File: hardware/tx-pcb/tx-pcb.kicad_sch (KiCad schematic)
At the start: 0 parts

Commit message: WIP TX Board
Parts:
- added C1, C11, C17, C2, C3, C4, C5, C8: 100n, symbol Device:C
- added C12, C6, C7: 4u7, symbol Device:C
- added C13: 100p, symbol Device:C
- added C14, C15: C, symbol Device:C
- added C16: 1u, symbol Device:C
- added FL1: MLPF-WB55-01E3, easyeda2kicad:FILTER-SMD_6P-L1.6-W1.0-P0.50-BL, symbol easyeda2kicad:MLPF-WB55-01E3
- added J1: TC2030, Connector:Tag-Connect_TC2030-IDC-FP_2x03_P1.27mm_Vertical, symbol Connector:Conn_ARM_SWD_TagConnect_TC2030
- added J2: CC1101_RF_Module_Conn, symbol Connector_Generic:Conn_02x04_Odd_Even
- added J3: USB2.0_C_16P, symbol Connector:USB_C_Receptacle_USB2.0_16P
- added L1: 10n, symbol Device:L
- added L2: 10u, symbol Device:L
- added R1, R3, R4: 5k1, symbol Device:R
- added R2: 100R, symbol Device:R
- added SW1: SW_Push, symbol Switch:SW_Push
- added U1: STM32WB55CEUx, Package_DFN_QFN:QFN-48-1EP_7x7mm_P0.5mm_EP5.6x5.6mm, symbol MCU_ST_STM32WB:STM32WB55CEUx
- added U2: USBLC6-2SC6, Package_TO_SOT_SMD:SOT-23-6, symbol Power_Protection:USBLC6-2SC6
- added X1: NX2016SA-32MHZ-STD-CZS-5, easyeda2kicad:OSC-SMD_4P-L2.0-W1.6-BL, symbol easyeda2kicad:NX2016SA-32MHZ-STD-CZS-5
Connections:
- new net: J3.A5 (CC1), R4.1
- new net: J3.A6 (D+), J3.B6 (D+), U2.3 (I/O2)
- new net: J3.A7 (D-), J3.B7 (D-), U2.1 (I/O1)
- new net: J3.B5 (CC2), R3.1
- new net: R2.2, SW1.1
- new net: J1.2 (SWDIO), U1.39 (PA13)
- new net: J1.4 (SWCLK), U1.41 (PA14)
- new net: J1.6 (SWO), U1.43 (PB3)
- new net +3V3: C1.1, C11.1, C13.1, C2.1, C3.1, C4.1, C5.1, C6.1, C7.1, C8.1, J1.1 (VCC), J2.2 (Pin_2), SW1.2, U1.1 (VBAT), U1.20 (VDD), U1.23 (VDDRF), U1.34 (VDDSMPS), U1.35 (VDD), U1.40 (VDDUSB), U1.48 (VDD), U1.8 (VDDA)
- new net +5V: J3.A4 (VBUS), J3.A9 (VBUS), J3.B4 (VBUS), J3.B9 (VBUS), U2.5 (VBUS)
- new net BOOT0: C17.2, R1.1, R2.1, U1.4 (PH3)
- new net C1101_CSN: J2.4 (Pin_4)
- new net C1101_GD02: J2.8 (Pin_8)
- new net C1101_GDO0: J2.3 (Pin_3)
- new net C1101_MISO/GD01: J2.7 (Pin_7)
- new net C1101_MOSI: J2.6 (Pin_6)
- new net C1101_SCK: J2.5 (Pin_5)
- new net GND: C1.2, C11.2, C12.2, C13.2, C14.2, C15.2, C16.2, C17.1, C2.2, C3.2, C4.2, C5.2, C6.2, C7.2, C8.2, FL1.2 (GND4), FL1.4 (GND1), FL1.5 (GND2), FL1.6 (GND3), J1.5 (GND), J2.1 (Pin_1), J3.A1 (GND), J3.A12 (GND), J3.B1 (GND), J3.B12 (GND), J3.SH (SHIELD), R1.2, R3.2, R4.2, U1.22 (VSSRF), U1.32 (VSSSMPS), U1.49 (VSS), U2.2 (GND), X1.2 (GND), X1.4 (GND)
- new net HSE_OSC_IN: U1.25 (OSC_IN), X1.1
- new net HSE_OSC_OUT: U1.24 (OSC_OUT), X1.3
- new net LSE_OSC_IN: C15.1, U1.2 (PC14)
- new net LSE_OSC_OUT: C14.1, U1.3 (PC15)
- new net RF1_IN: FL1.3 (IN), U1.21 (RF1)
- new net SMPSFB: C12.1, L2.2, U1.31 (VFBSMPS)
- new net SMPSLX: L1.1, U1.33 (VLXSMPS)
- new net SMPSLXL: L1.2, L2.1
- new net SWD_NSRT: C16.1, J1.3 (~{RESET}), U1.7 (NRST)
- new net USB_DM: U1.37 (PA11), U2.6 (I/O1)
- new net USB_DP: U1.38 (PA12), U2.4 (I/O2)
- no-connect marks 0 -> 2
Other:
- added sheet Power (Power.kicad_sch)
- note added: "5k1 R's tell the computer there is a power-sinking device connected"
- note added: "ESD Protection"
- note added: "From STM application note an5165 STM32WB55xx 6.1.6 Fig 16"
- note added: "MLFP-WB55-01D3 / -01E3 ?"
- note added: "Refer to AN6335 for trace Z"
- note added: "ST DESIGN NOTE AN2867"
- note added: "debounce; det vals"
- note added: "match with TX?"
- company: (none) -> University of Central Florida Student Group
- title: (none) -> Transceiver Demo Board

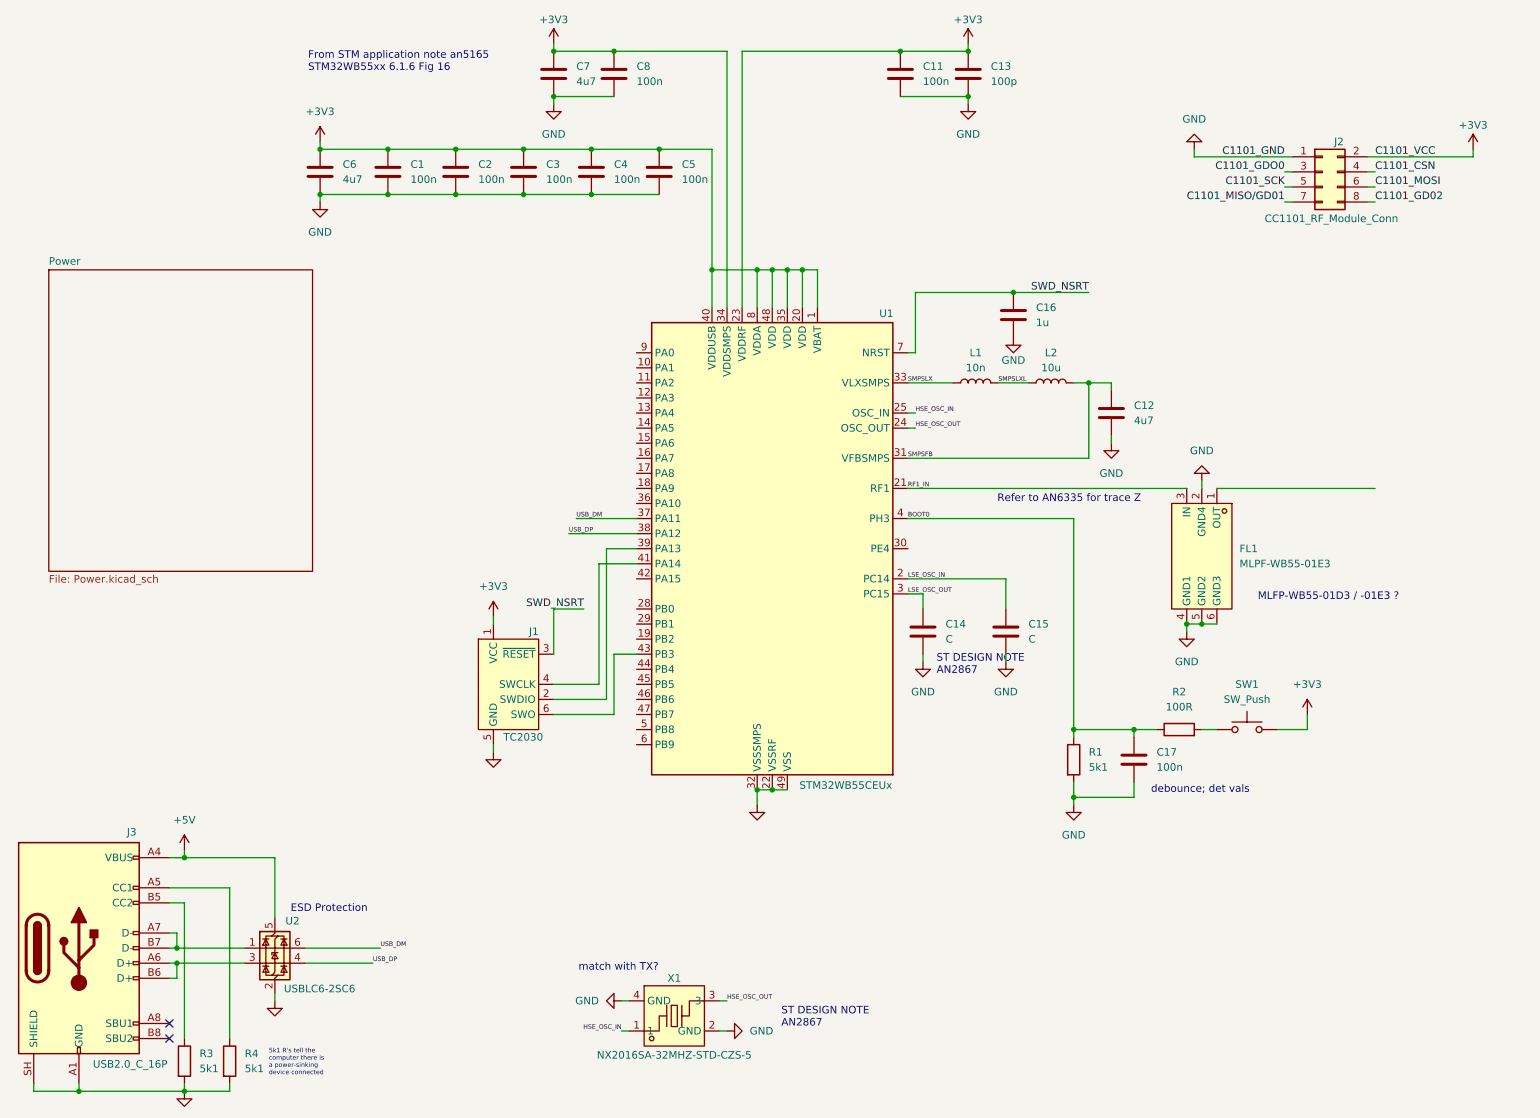
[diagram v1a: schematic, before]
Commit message: began work on RF daughter board; included TI Reference designs
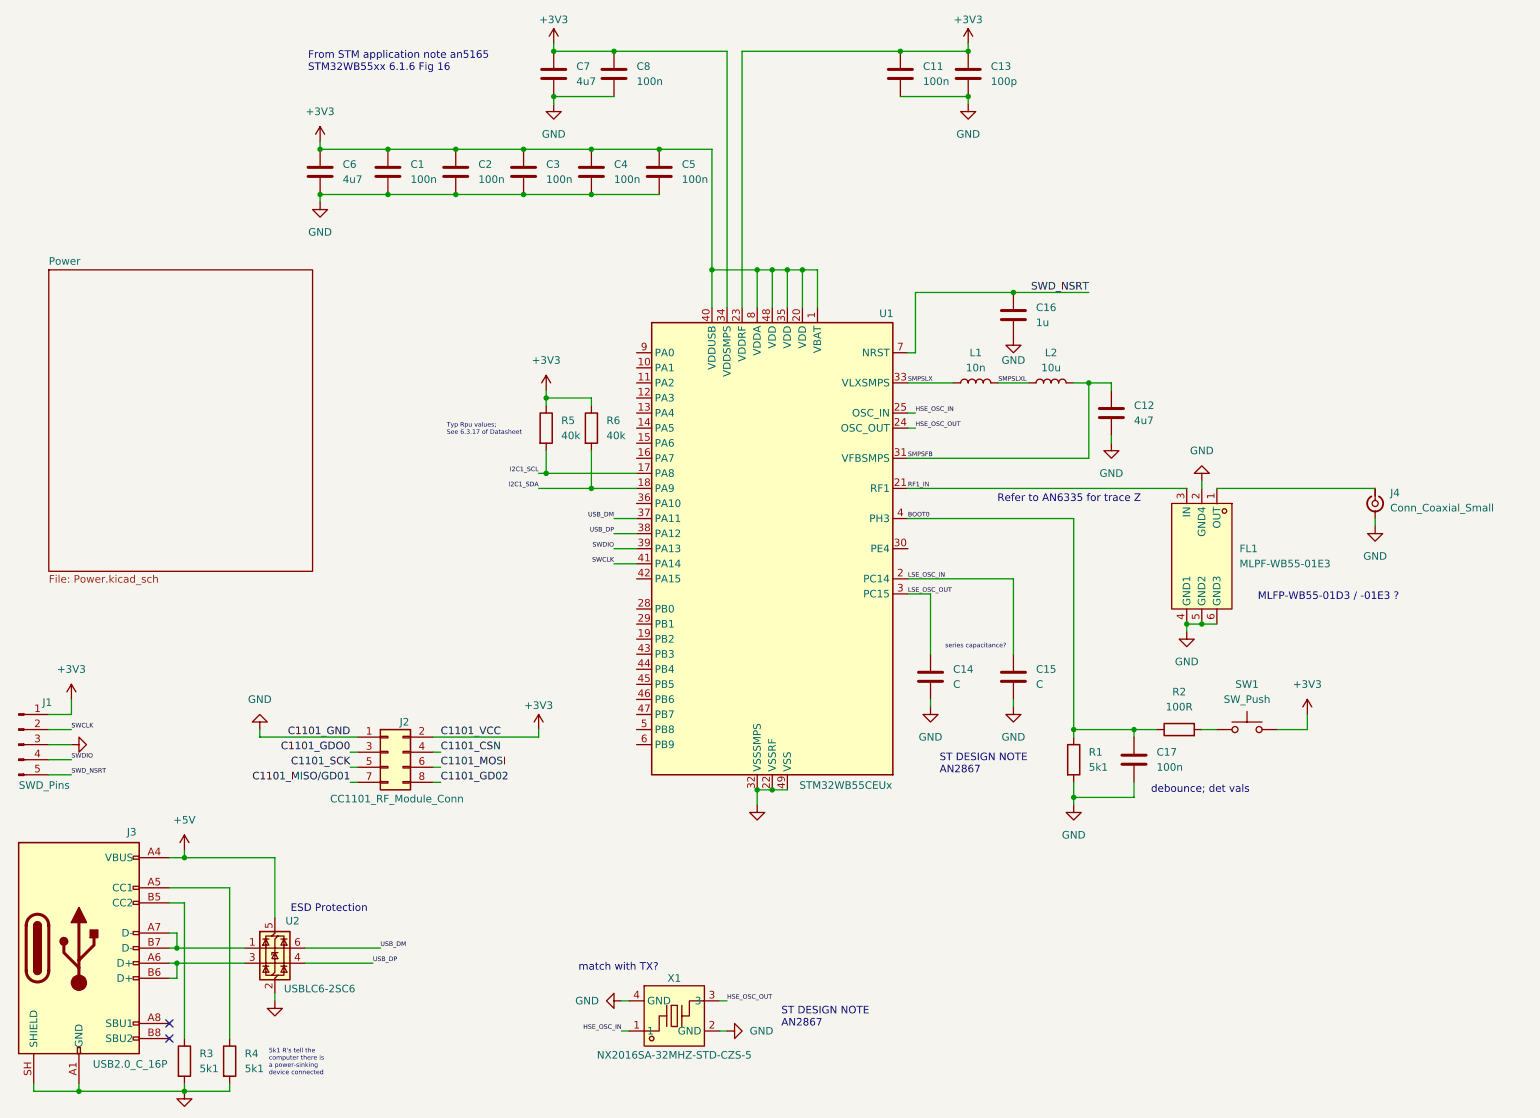
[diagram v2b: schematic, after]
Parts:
- removed J1: TC2030, Connector:Tag-Connect_TC2030-IDC-FP_2x03_P1.27mm_Vertical, symbol Connector:Conn_ARM_SWD_TagConnect_TC2030
- added J1: SWD_Pins, symbol Connector:Conn_01x05_Pin
- added J4: Conn_Coaxial_Small, symbol Connector:Conn_Coaxial_Small
- added R5, R6: 40k, symbol Device:R
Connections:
- net +3V3: now also J1.1 (Pin_1), R5.1, R6.1
- net GND: now also J1.3 (Pin_3), J4.2 (Ext)
- net SWD_NSRT: now also J1.5 (Pin_5)
- net I2C1_SCL: now reaches U1.17 (PA8)
- net I2C1_SCL: now also R5.2
- net I2C1_SDA: now reaches U1.18 (PA9)
- net I2C1_SDA: now also R6.2
- net SWDIO: now reaches U1.39 (PA13)
- net SWDIO: now also J1.4 (Pin_4)
- net SWCLK: now reaches U1.41 (PA14)
- net SWCLK: now also J1.2 (Pin_2)
- net at FL1.1 (OUT): now also J4.1 (In)
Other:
- note added: "Typ Rpu values; See 6.3.17 of Datasheet"
- note added: "series capacitance?"
- moved on the sheet: C14, C15, J2
